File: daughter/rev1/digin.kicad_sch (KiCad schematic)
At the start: 17 parts, among them U41 TXUN0104RUTR, U42 ADUM5242ARZ, U43 ADUM5242ARZ

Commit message: Rename versions
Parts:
- U42, U43: footprint myparts:R_8_ADI -> myparts:R_8_ADI-M
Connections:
- net +1.8V renamed +1V8
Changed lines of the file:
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@@
+	)
+	(symbol
+		(lib_id "power:+1V8")
+		(at 36.83 74.93 0)
+		(unit 1)
+		(exclude_from_sim no)
+		(in_bom yes)
+		(on_board yes)
+		(dnp no)
+		(fields_autoplaced yes)
+		(property "Reference" "#PWR0277"
+			(at 36.83 78.74 0)
+			(effects
+				(font
+					(size 1.27 1.27)
+				)
+				(hide yes)
+			)
+		)
+		(property "Value" "+1V8"
+			(at 36.83 69.85 0)
+			(effects
+				(font
+					(size 1.27 1.27)
+				)
+			)
+		)
+		(property "Footprint" ""
+			(at 36.83 74.93 0)
+			(effects
+				(font
+					(size 1.27 1.27)
+				)
+				(hide yes)
+			)
+		)
+		(property "Datasheet" ""
+			(at 36.83 74.93 0)
+			(effects
+				(font
+					(size 1.27 1.27)
+				)
+				(hide yes)
+			)
+		)
+		(property "Description" "Power symbol creates a global label with name \"+1V8\""
+			(at 36.83 74.93 0)
+			(effects
+				(font
+					(size 1.27 1.27)
+				)
+				(hide yes)
+			)
+		)
+		(pin "1"
+		)
+		(instances
+			(project "psc_daughter_brd"
+				(path "/40891cc8-bf64-41f4-8f69-a607d7b280eb/979dab62-5512-4152-97ee-117138a961d3/e0aa7f64-0a32-4be9-b0d8-80395ba4c75d"
+					(reference "#PWR0277")
+					(unit 1)
+				)
+			)
+		)
 	)
 	(symbol
@@
 		(dnp no)
 		(property "Reference" "U41"
-			(at 70.358 108.204 0)
+			(at 64.77 80.01 0)
 			(effects
 				(font
@@
 		)
 		(property "Value" "TXUN0104RUTR"
-			(at 64.77 84.328 0)
+			(at 64.77 82.55 0)
 			(effects
 				(font
@@
 			)
 		)
-		(property "Footprint" "myparts:R_8_ADI"
+		(property "Footprint" "myparts:R_8_ADI-M"
 			(at 127 50.8 0)
 			(effects
@@
 			)
 		)
-		(property "Footprint" "myparts:R_8_ADI"
+		(property "Footprint" "myparts:R_8_ADI-M"
 			(at 127 120.65 0)
 			(effects
@@
 					(unit 1)
 				)
-			)
-		)
-	)
-	(symbol
-		(lib_id "PSC:+1.8V")
-		(at 36.83 74.93 0)
-		(unit 1)
-		(exclude_from_sim no)
-		(in_bom yes)
-		(on_board yes)
-		(dnp no)
-		(property "Reference" "#PWR054"
-			(at 36.83 78.74 0)
-			(effects
-				(font
-					(size 1.27 1.27)
-				)
-				(hide yes)
-			)
-		)
-		(property "Value" "+1.8V"
-			(at 36.83 69.85 0)
-			(effects
-				(font
-					(size 1.27 1.27)
-				)
-			)
-		)
-		(property "Footprint" ""
-			(at 36.83 74.93 0)
-			(effects
-				(font
-					(size 1.27 1.27)
-				)
-				(hide yes)
-			)
-		)
-		(property "Datasheet" ""
-			(at 36.83 74.93 0)
-			(effects
-				(font
-					(size 1.27 1.27)
-				)
-				(hide yes)
-			)
-		)
-		(property "Description" ""
-			(at 36.83 74.93 0)
-			(effects
-				(font
-					(size 1.27 1.27)
-				)
-				(hide yes)
-			)
-		)
-		(pin "1"
-		)
-		(instances
-			(project "psc_daughter_brd"
-				(path "/40891cc8-bf64-41f4-8f69-a607d7b280eb/979dab62-5512-4152-97ee-117138a961d3/e0aa7f64-0a32-4be9-b0d8-80395ba4c75d"
-					(reference "#PWR054")
-					(unit 1)
-				)

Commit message: Change adc driver to ADA4945
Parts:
- U42, U43: footprint myparts:R_8_ADI-M -> myparts:R_8_ADI
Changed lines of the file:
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@@
 			)
 		)
-		(property "Footprint" "myparts:R_8_ADI-M"
+		(property "Footprint" "myparts:R_8_ADI"
 			(at 127 50.8 0)
 			(effects
@@
 			)
 		)
-		(property "Footprint" "myparts:R_8_ADI-M"
+		(property "Footprint" "myparts:R_8_ADI"
 			(at 127 120.65 0)
 			(effects

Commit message: u41 was pulled up to non-existent voltage +1V8 changed +1.8V
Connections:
- net +1V8 renamed +1.8V
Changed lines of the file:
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@@
-	)
-	(symbol
-		(lib_id "power:+1V8")
-		(at 36.83 74.93 0)
-		(unit 1)
-		(exclude_from_sim no)
-		(in_bom yes)
-		(on_board yes)
-		(dnp no)
-		(fields_autoplaced yes)
-		(property "Reference" "#PWR0277"
-			(at 36.83 78.74 0)
-			(effects
-				(font
-					(size 1.27 1.27)
-				)
-				(hide yes)
-			)
-		)
-		(property "Value" "+1V8"
-			(at 36.83 69.85 0)
-			(effects
-				(font
-					(size 1.27 1.27)
-				)
-			)
-		)
-		(property "Footprint" ""
-			(at 36.83 74.93 0)
-			(effects
-				(font
-					(size 1.27 1.27)
-				)
-				(hide yes)
-			)
-		)
-		(property "Datasheet" ""
-			(at 36.83 74.93 0)
-			(effects
-				(font
-					(size 1.27 1.27)
-				)
-				(hide yes)
-			)
-		)
-		(property "Description" "Power symbol creates a global label with name \"+1V8\""
-			(at 36.83 74.93 0)
-			(effects
-				(font
-					(size 1.27 1.27)
-				)
-				(hide yes)
-			)
-		)
-		(pin "1"
-		)
-		(instances
-			(project "psc_daughter_brd"
-				(path "/40891cc8-bf64-41f4-8f69-a607d7b280eb/979dab62-5512-4152-97ee-117138a961d3/e0aa7f64-0a32-4be9-b0d8-80395ba4c75d"
-					(reference "#PWR0277")
-					(unit 1)
-				)
-			)
-		)
 	)
 	(symbol
@@
 					(unit 1)
 				)
+			)
+		)
+	)
+	(symbol
+		(lib_id "PSC:+1.8V")
+		(at 36.83 74.93 0)
+		(unit 1)
+		(exclude_from_sim no)
+		(in_bom yes)
+		(on_board yes)
+		(dnp no)
+		(property "Reference" "#PWR054"
+			(at 36.83 78.74 0)
+			(effects
+				(font
+					(size 1.27 1.27)
+				)
+				(hide yes)
+			)
+		)
+		(property "Value" "+1.8V"
+			(at 36.83 69.85 0)
+			(effects
+				(font
+					(size 1.27 1.27)
+				)
+			)
+		)
+		(property "Footprint" ""
+			(at 36.83 74.93 0)
+			(effects
+				(font
+					(size 1.27 1.27)
+				)
+				(hide yes)
+			)
+		)
+		(property "Datasheet" ""
+			(at 36.83 74.93 0)
+			(effects
+				(font
+					(size 1.27 1.27)
+				)
+				(hide yes)
+			)
+		)
+		(property "Description" ""
+			(at 36.83 74.93 0)
+			(effects
+				(font
+					(size 1.27 1.27)
+				)
+				(hide yes)
+			)
+		)
+		(pin "1"
+		)
+		(instances
+			(project "psc_daughter_brd"
+				(path "/40891cc8-bf64-41f4-8f69-a607d7b280eb/979dab62-5512-4152-97ee-117138a961d3/e0aa7f64-0a32-4be9-b0d8-80395ba4c75d"
+					(reference "#PWR054")
+					(unit 1)
+				)

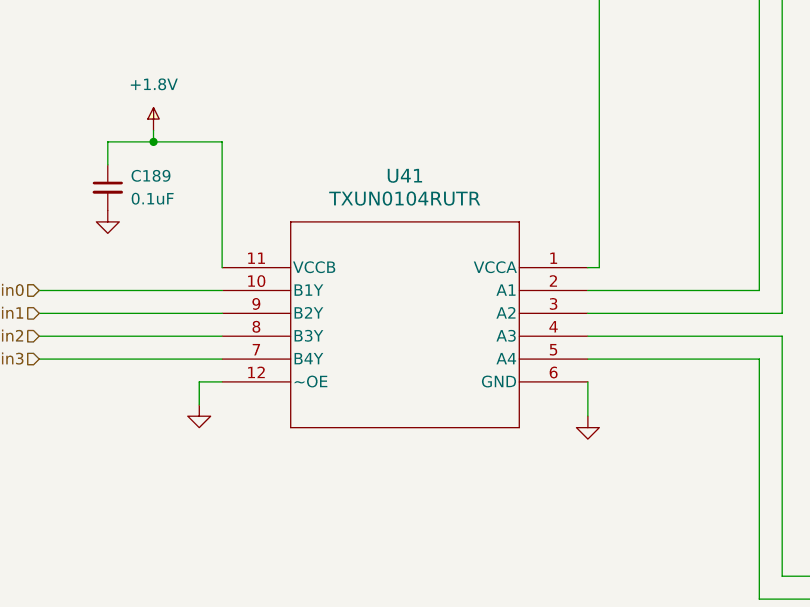
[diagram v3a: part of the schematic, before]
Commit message: Finish routing of daughterboard
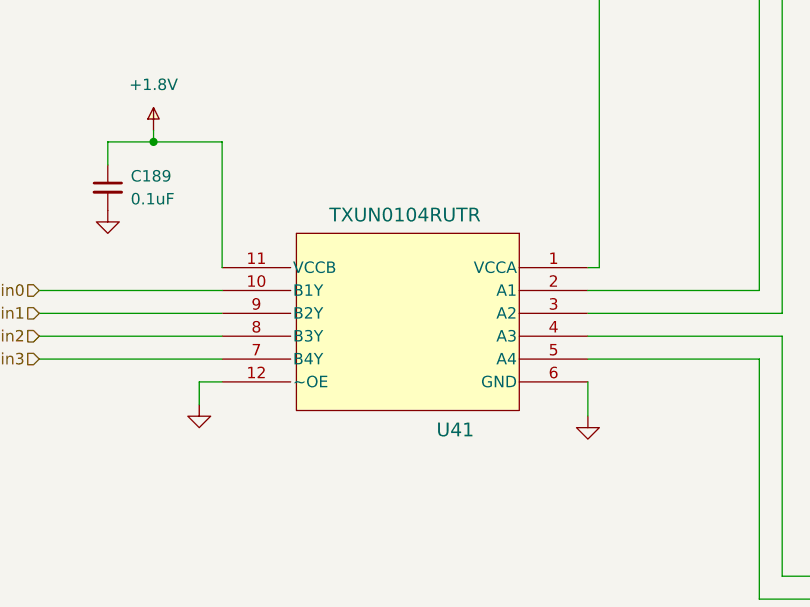
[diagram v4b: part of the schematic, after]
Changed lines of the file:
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@@
 		(dnp no)
 		(property "Reference" "U41"
-			(at 64.77 80.01 0)
+			(at 70.358 108.204 0)
 			(effects
 				(font
@@
 		)
 		(property "Value" "TXUN0104RUTR"
-			(at 64.77 82.55 0)
+			(at 64.77 84.328 0)
 			(effects
 				(font
